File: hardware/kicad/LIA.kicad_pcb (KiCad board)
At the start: 2 copper layers, 79 x 30 mm, 81 parts, among them J2 POGO-4P-FEM, Q1 8205A, Q2 AO3400A, Q3 AO3400A, Q4 AO3400A, U1 ESP32-S3-MINI-1-N8, U10 DW01A, U11 RT9080-33GJ5, U2 SAM-M10Q-00B, U3 Wio-SX1262, U5 TPD2EUSB30, U6 TYPE-C_16PIN_2MD(073), U7 RT9080-33GJ5, U8 TP4056, U9 MAX17048G+T10

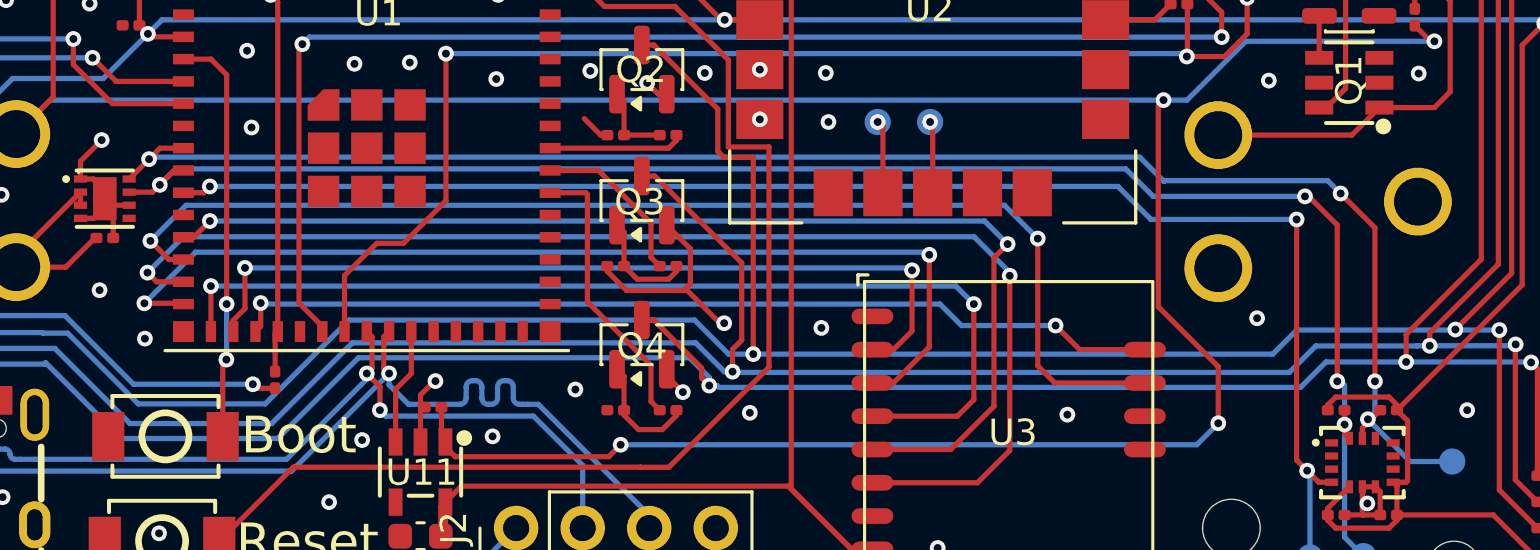
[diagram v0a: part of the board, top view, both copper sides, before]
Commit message: SDA/SCL corrected on IMU
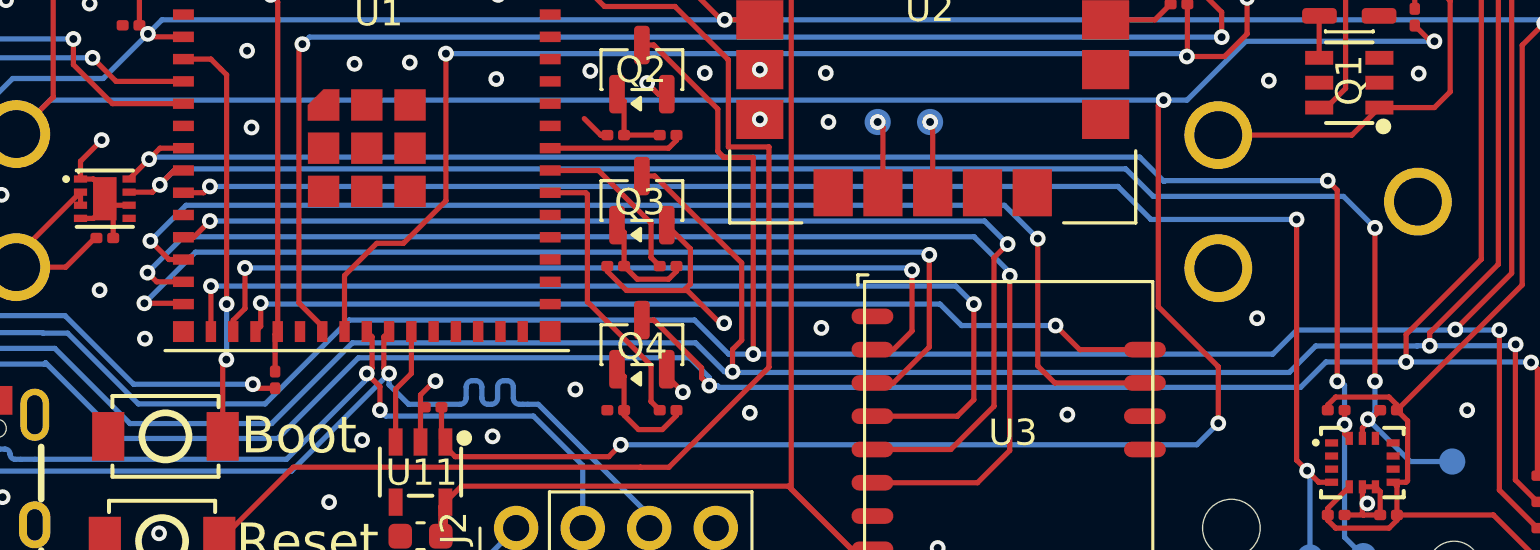
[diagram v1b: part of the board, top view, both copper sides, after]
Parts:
- LED1, LED2, LED3, LED4: value ~ -> MHS110CRGBCT
- PB1, PB2: value TS-1187A-B-A-B -> TS-1088-AR02016
- SW1: value ~ -> SSSS223900
- U12: value ~ -> LSM6DSOXTR
- renumbered SDA1 to SCL1, SCL1 to SDA1
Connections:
- R4 pad 2: SDA -> SCL
- R5 pad 2: SCL -> SDA
- SCL1 pad 1: SDA -> SCL
- SDA1 pad 1: SCL -> SDA
- U12 pad 13: SDA -> SCL
- U12 pad 14: SCL -> SDA
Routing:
- net SDA: track 63.2 -> 64.1 mm
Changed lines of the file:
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@@
 			)
 		)
-		(property "Value" "TS-1187A-B-A-B"
+		(property "Value" "TS-1088-AR02016"
 			(at 0 2.4655 0)
 			(layer "F.Fab")
@@
 			)
 		)
-		(property "Value" "~"
+		(property "Value" "SSSS223900"
 			(at -0.014967 5.157433 0)
 			(layer "F.Fab")
@@
 			(layers "F.Cu" "F.Mask")
 			(roundrect_rratio 0.25)
-			(net 59 "SDA")
+			(net 60 "SCL")
 			(pintype "passive")
 		)
@@
 			)
 		)
-		(property "Value" "~"
+		(property "Value" "MHS110CRGBCT"
 			(at 0 2.215747 50)
 			(layer "F.Fab")
@@
 			)
 		)
-		(property "Value" "~"
+		(property "Value" "MHS110CRGBCT"
 			(at 0 2.215747 130)
 			(layer "F.Fab")
@@
 			(layers "F.Cu" "F.Mask")
 			(roundrect_rratio 0.25)
-			(net 60 "SCL")
+			(net 59 "SDA")
 			(pintype "passive")
 		)
@@
 			)
 		)
-		(property "Value" "TS-1187A-B-A-B"
+		(property "Value" "TS-1088-AR02016"
 			(at 0 2.4655 0)
 			(layer "F.Fab")
@@
 			)
 		)
-		(property "Value" "~"
+		(property "Value" "MHS110CRGBCT"
 			(at 0 2.215747 130)
 			(layer "F.Fab")
@@
 			)
 		)
-		(property "Value" "~"
+		(property "Value" "LSM6DSOXTR"
 			(at -0.06375 2.2505 0)
 			(layer "F.Fab")
@@
 			(size 0.28 0.5)
 			(layers "F.Cu" "F.Mask" "F.Paste")
-			(net 59 "SDA")
+			(net 60 "SCL")
 			(pinfunction "SCL")
 			(pintype "unspecified")
@@
 			(size 0.28 0.5)
 			(layers "F.Cu" "F.Mask" "F.Paste")
-			(net 60 "SCL")
+			(net 59 "SDA")
 			(pinfunction "SDA")
 			(pintype "unspecified")
@@
 			)
 		)
-		(property "Value" "~"
+		(property "Value" "MHS110CRGBCT"
 			(at 0 2.215747 50)
 			(layer "F.Fab")
@@
 		(descr "SMD pad as test Point, diameter 1.0mm")
 		(tags "test point SMD pad")
-		(property "Reference" "SDA1"
+		(property "Reference" "SCL1"
 			(at 0 1.448 0)
 			(layer "B.SilkS")
@@
 			(size 1 1)
 			(layers "B.Cu" "B.Mask")
-			(net 59 "SDA")
+			(net 60 "SCL")
 			(pinfunction "1")
 			(pintype "passive")
@@
 		(descr "SMD pad as test Point, diameter 1.0mm")
 		(tags "test point SMD pad")
-		(property "Reference" "SCL1"
+		(property "Reference" "SDA1"
 			(at -1.77 1.33 0)
 			(layer "B.SilkS")
@@
 			(size 1 1)
 			(layers "B.Cu" "B.Mask")
-			(net 60 "SCL")
+			(net 59 "SDA")
 			(pinfunction "1")
 			(pintype "passive")
@@
 		)
 	)
-	(gr_text "SCL\n"
+	(gr_text "SDA"
 		(at 187.71 105.41 0)
 		(layer "B.SilkS")
@@
 		)
 	)
-	(gr_text "SDA\n"
+	(gr_text "SCL\n"
 		(at 192.76 103.56 0)
 		(layer "B.SilkS")
@@
 	)
 	(segment
-		(start 187.48 100.399)
-		(end 187.48 94.54)
+		(start 186.04 93.1)
+		(end 185.679 92.739)
+		(width 0.2)
+		(layer "F.Cu")
+		(net 59)
+	)
+	(segment
+		(start 186.32 102.14)
+		(end 186.32 102.395)
 		(width 0.2)
 		(layer "F.Cu")
@@
 	)
 	(segment
-		(start 187.48 94.54)
-		(end 186.17 93.23)
+		(start 186.04 100.397175)
+		(end 186.04 93.1)
 		(width 0.2)
 		(layer "F.Cu")
@@
 	)
 	(segment
-		(start 187 102.18)
-		(end 187 102.575)
+		(start 141.105156 91.5)
+		(end 142 91.5)
 		(width 0.2)
 		(layer "F.Cu")
@@
 	)
 	(segment
-		(start 141.105156 91.5)
-		(end 142 91.5)
+		(start 186.32 102.395)
+		(end 186.5 102.575)
 		(width 0.2)
 		(layer "F.Cu")
@@
 	)
 	(segment
-		(start 187.68 101.5)
-		(end 187 102.18)
+		(start 186.32 101.5)
+		(end 186.32 102.14)
+		(width 0.2)
+		(layer "F.Cu")
+		(net 59)
+	)
+	(segment
+		(start 186.041825 100.399)
+		(end 186.04 100.397175)
 		(width 0.2)
 		(layer "F.Cu")
@@
 	)
 	(via
-		(at 187.211215 101.847648)
+		(at 186.32 102.05)
 		(size 0.6)
 		(drill 0.3)
@@
 	)
 	(via
-		(at 186.17 93.23)
+		(at 186.041825 100.399)
 		(size 0.6)
 		(drill 0.3)
@@
 	)
 	(via
-		(at 187.48 100.399)
+		(at 140.687578 91.917578)
 		(size 0.6)
 		(drill 0.3)
@@
 	)
 	(via
-		(at 140.687578 91.917578)
+		(at 185.679 92.739)
 		(size 0.6)
 		(drill 0.3)
@@
 	)
 	(segment
-		(start 188.823567 103.46)
-		(end 187.211215 101.847648)
+		(start 186.041825 100.399)
+		(end 186.169 100.399)
 		(width 0.2)
 		(layer "B.Cu")
@@
 	)
 	(segment
-		(start 179.43 92.77)
-		(end 179.461 92.739)
+		(start 187.04 107.07)
+		(end 186.32 106.35)
 		(width 0.2)
 		(layer "B.Cu")
@@
 	)
 	(segment
-		(start 187.48 100.399)
-		(end 187.48 101.578863)
+		(start 186.169 100.399)
+		(end 186.32 100.55)
 		(width 0.2)
 		(layer "B.Cu")
@@
 	)
 	(segment
-		(start 185.679 92.739)
-		(end 186.17 93.23)
+		(start 179.43 92.77)
+		(end 179.461 92.739)
 		(width 0.2)
 		(layer "B.Cu")
@@
 	)
 	(segment
-		(start 178.5 91.84)
-		(end 179.43 92.77)
+		(start 186.32 106.35)
+		(end 186.32 102.05)
 		(width 0.2)
 		(layer "B.Cu")
@@
 	)
 	(segment
-		(start 190.43 103.46)
-		(end 188.823567 103.46)
+		(start 178.5 91.84)
+		(end 179.43 92.77)
 		(width 0.2)
 		(layer "B.Cu")
@@
 	)
 	(segment
-		(start 187.48 101.578863)
-		(end 187.211215 101.847648)
+		(start 186.32 100.55)
+		(end 186.32 102.05)
 		(width 0.2)
 		(layer "B.Cu")
@@
 	)
 	(segment
-		(start 184.95 93.34)
-		(end 184.81 93.34)
-		(width 0.2)
-		(layer "F.Cu")
-		(net 60)
-	)
-	(segment
-		(start 186.32 102.14)
-		(end 186.32 102.395)
+		(start 187.48 100.399)
+		(end 187.48 94.54)
 		(width 0.2)
 		(layer "F.Cu")
@@
 	)
 	(segment
-		(start 186.04 100.397175)
-		(end 186.04 94.43)
-		(width 0.2)
-		(layer "F.Cu")
-		(net 60)
-	)
-	(segment
-		(start 186.04 94.43)
-		(end 184.95 93.34)
+		(start 187 102.18)
+		(end 187 102.575)
 		(width 0.2)
 		(layer "F.Cu")
@@
 	)
 	(segment
-		(start 186.32 102.395)
-		(end 186.5 102.575)
-		(width 0.2)
-		(layer "F.Cu")
-		(net 60)
-	)
-	(segment
 		(start 141.648 92.35)
 		(end 142 92.35)
@@
 	)
 	(segment
-		(start 139.92761 93.177674)
-		(end 140.820326 93.177674)
-		(width 0.2)
-		(layer "F.Cu")
-		(net 60)
-	)
-	(segment
-		(start 186.32 101.5)
-		(end 186.32 102.14)
+		(start 187.68 101.5)
+		(end 187 102.18)
 		(width 0.2)
 		(layer "F.Cu")
@@
 	)
 	(segment
-		(start 186.041825 100.399)
-		(end 186.04 100.397175)
+		(start 139.92761 93.177674)
+		(end 140.820326 93.177674)
 		(width 0.2)
 		(layer "F.Cu")
@@
 	)
 	(via
-		(at 141.099 92.899)
+		(at 187.211215 101.847648)
 		(size 0.6)
 		(drill 0.3)
@@
 	)
 	(via
-		(at 184.81 93.34)
+		(at 141.099 92.899)
 		(size 0.6)
 		(drill 0.3)
@@
 	)
 	(via
-		(at 186.32 102.05)
+		(at 187.48 94.54)
 		(size 0.6)
 		(drill 0.3)
@@
 	)
 	(via
-		(at 186.041825 100.399)
+		(at 187.48 100.399)
 		(size 0.6)
 		(drill 0.3)
@@
 	)
 	(segment
-		(start 141.708 92.29)
-		(end 141.099 92.899)
+		(start 188.823567 103.46)
+		(end 187.211215 101.847648)
 		(width 0.2)
 		(layer "B.Cu")
@@
 	)
 	(segment
-		(start 186.041825 100.399)
-		(end 186.169 100.399)
+		(start 179.0171 93.34)
+		(end 186.28 93.34)
 		(width 0.2)
 		(layer "B.Cu")
@@
 	)
 	(segment
-		(start 184.81 93.34)
+		(start 177.9671 92.29)
 		(end 179.0171 93.34)
 		(width 0.2)
@@
 	)
 	(segment
-		(start 187.04 107.07)
-		(end 186.32 106.35)
+		(start 187.48 100.399)
+		(end 187.48 101.578863)
 		(width 0.2)
 		(layer "B.Cu")
@@
 	)
 	(segment
-		(start 186.169 100.399)
-		(end 186.32 100.55)
+		(start 190.43 103.46)
+		(end 188.823567 103.46)
 		(width 0.2)
 		(layer "B.Cu")
@@
 	)
 	(segment
-		(start 179.0171 93.34)
-		(end 177.9671 92.29)
+		(start 141.099 92.899)
+		(end 141.708 92.29)
 		(width 0.2)
 		(layer "B.Cu")
@@
 	)
 	(segment
-		(start 177.9671 92.29)
-		(end 141.708 92.29)
+		(start 187.48 101.578863)
+		(end 187.211215 101.847648)
 		(width 0.2)
 		(layer "B.Cu")
@@
 	)
 	(segment
-		(start 186.32 106.35)
-		(end 186.32 102.05)
+		(start 186.28 93.34)
+		(end 187.48 94.54)
 		(width 0.2)
 		(layer "B.Cu")
@@
 	)
 	(segment
-		(start 186.32 100.55)
-		(end 186.32 102.05)
+		(start 141.708 92.29)
+		(end 177.9671 92.29)
 		(width 0.2)
 		(layer "B.Cu")
